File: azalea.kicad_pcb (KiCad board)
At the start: 4 copper layers, 70.6 x 53.3 mm, 103 parts, among them J1 NEIGHBOR1, J2 NEIGHBOR2, J3 USB-MICRO-B-SHIELDED, J4 USB-MICRO-B-SHIELDED, J5 JTAG, J6 POWER, J7 BONUS_ROW, SW1 DFU, SW2 RESET, U1 LPC4330FBD144, U2 W25Q16DV, U3 AP7333, U4 IP4220CZ6, U5 AP2553W6-7, X1 MCU_XTAL, X2 RTC_XTAL

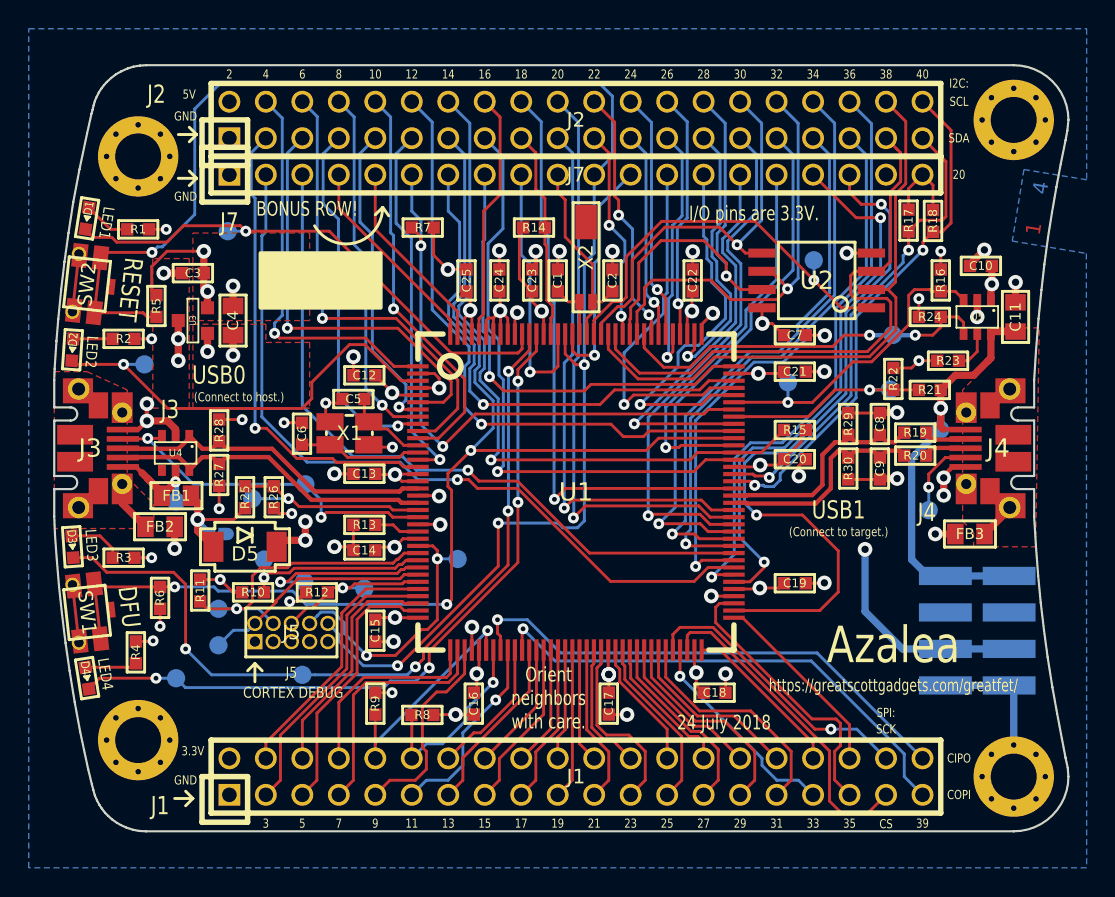
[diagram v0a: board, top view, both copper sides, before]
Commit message: pcb: rev 1
- Cortex debug header changed to 2mm
- Adjusted the silkscreen

Signed-off-by: Filipe Laíns <lains@archlinux.org>
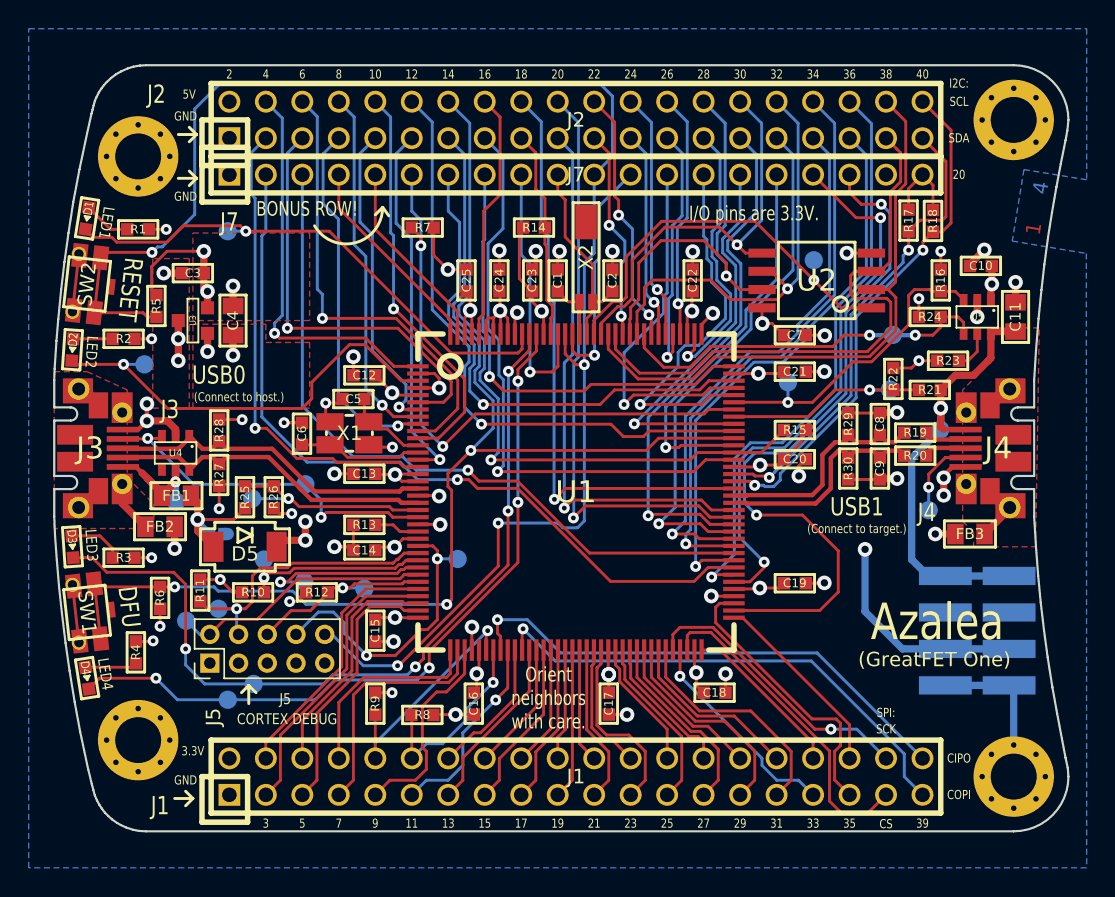
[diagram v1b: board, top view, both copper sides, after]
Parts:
- added G***: LOGO, ffy00-modules:brasao-smaller, B.Cu at (146.1, 100.6)
- J5: footprint gsg-modules:50MIL-HEADER-2x5-TH -> Connector_PinHeader_2.00mm:PinHeader_2x05_P2.00mm_Vertical
- moved J5 6.07 mm to (116.8, 112.8), turned to 90 degrees
- moved TP6 3.90 mm to (118.0, 115.3)
- moved TP5 3.45 mm to (119.8, 114.2)
- moved TP16 2.82 mm to (115.1, 109.8)
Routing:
- net /TMS: track 16.0 -> 18.3 mm
- net /TDO: track 11.6 -> 13.6 mm
- net /TDI: track 19.6 -> 21.1 mm
- net /LED3: track 56.5 -> 57.7 mm
- net /TCK: track 22.3 -> 21.1 mm
- net /LED4: track 51.2 -> 51.9 mm
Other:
- net class Default removed
- board text added: "(GreatFET One)"
- board text added: "Don't trust atoms. They make up everything!"
- board text added: "Manufactured by Filipe Laíns @FFY00"
- board text removed: "24 July 2018"
- board text removed: "Keep hacking."
- board text removed: "https://greatscottgadgets.com/greatfet/"
